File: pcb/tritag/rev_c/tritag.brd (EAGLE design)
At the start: 61 x 34.5 mm, 139 parts, among them J1 TC2030-JLINK-NL, J2 TC2030-JLINK-NL, J3 MICRO_USB_B_HIROSE_ZX62-B-5PA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, J5 BAT_HOLE, J7 CON_MICRO_SDDM3AT-SF-PEJM5, T1 HHM1595A1, U1 NRF52840, U12 SIP32510, U2 MCP73831, U3 FT232RQ, U4 MAX8887EZK33+T, U5 STM32F091CC, U6 SKY13317, U7 LXDC2HN18A, U8 DW1000, U9 LIS2DW12, X1 32MHz, X2 38.4M, X3 16M, X4 32.768kHz

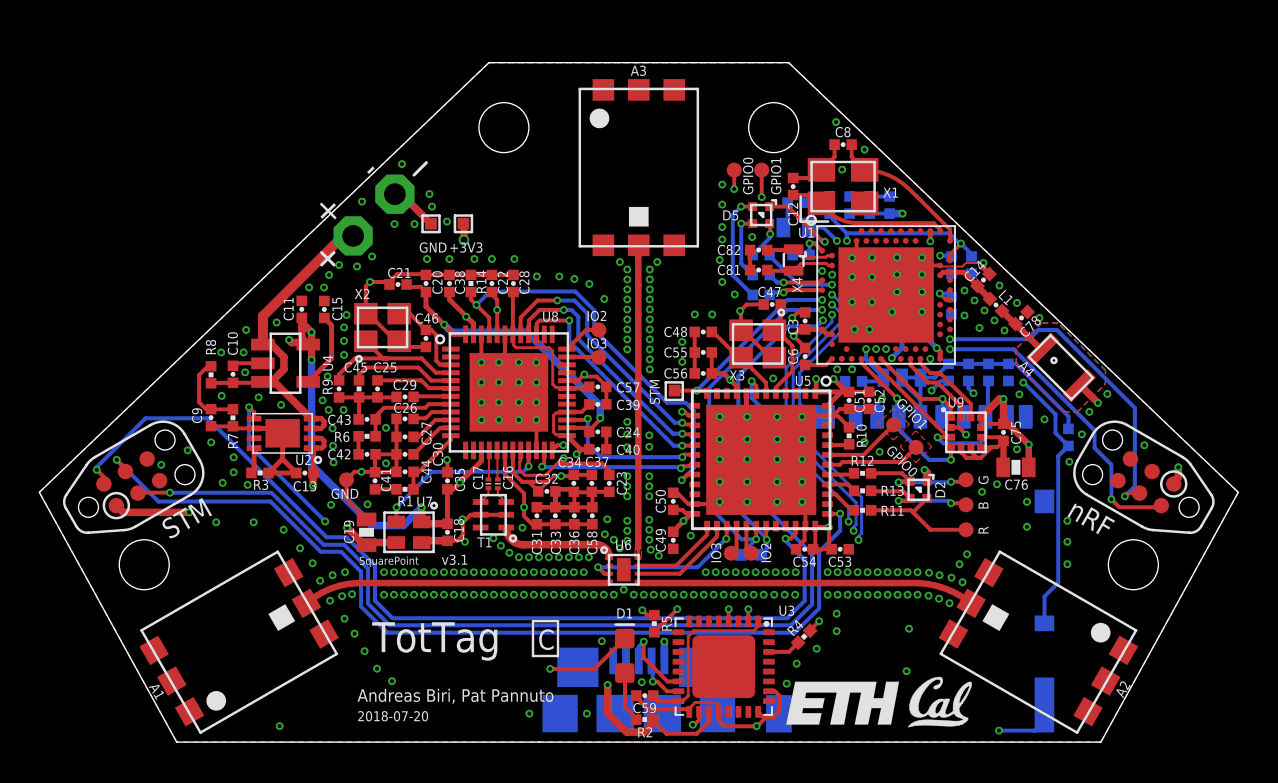
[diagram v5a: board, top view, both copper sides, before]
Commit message: renumbered parts, added decaps for power supply
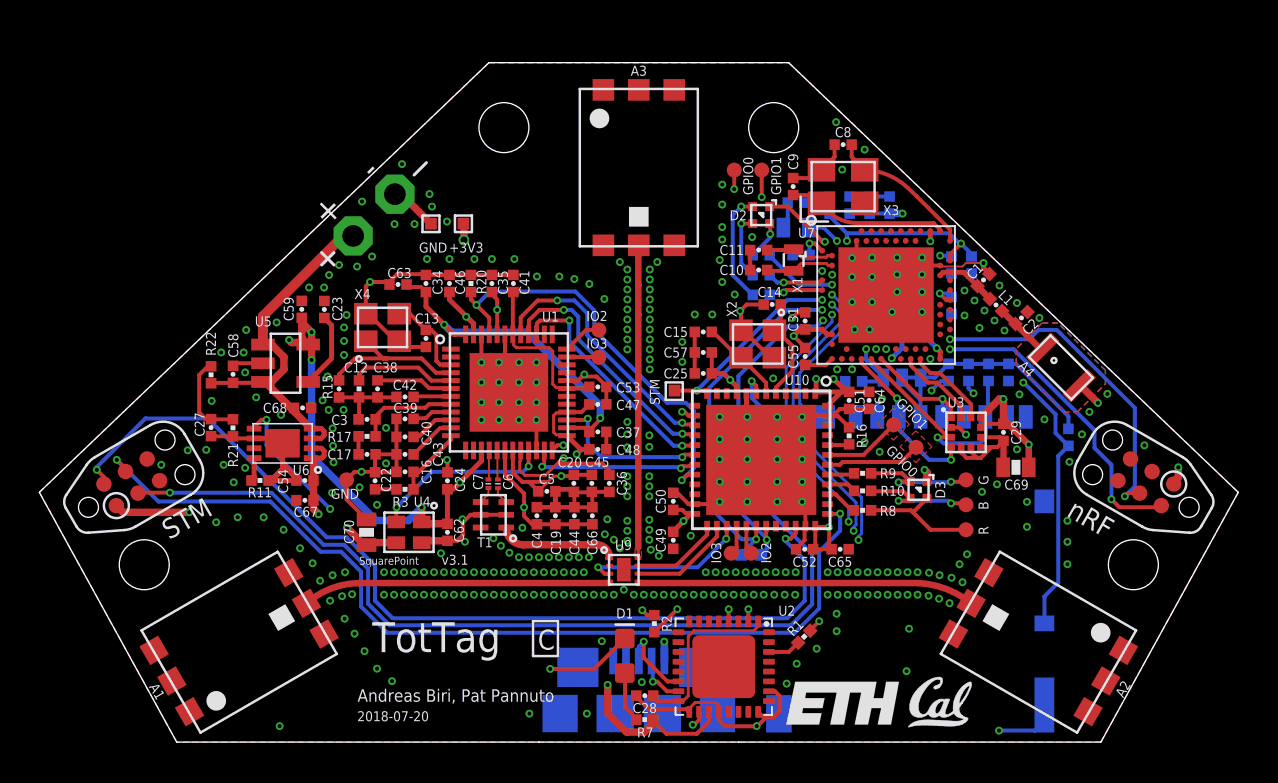
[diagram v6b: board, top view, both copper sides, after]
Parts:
- removed C75: 0.1uF, passives:0402_CAP
- removed C77: 4.7uF, passives:0402_CAP
- removed C78: 1pF, passives:0402_CAP
- removed C79: 1uF, passives:0402_CAP
- removed C80: 47nF, passives:0402_CAP
- removed C81, C82: 12pF, passives:0402_CAP
- removed D5: SML-LX0404SIUPGUSB, leds:1MM_SQ_4PAD
- removed J7: CON_MICRO_SDDM3AT-SF-PEJM5, connector:DM3AT-SF-PEJM5
- removed R23: 10k, passives:0402_RES
- removed R27, R28, R29: 470, passives:0402_RES
- removed U12: SIP32510, chips:TSOT23-6
- added C61, C62, C63, C64, C65, C66, C67, C68: 4.7uF, passives:0402_CAP
- added C70: 10uF, passives:0603_CAP
- added D3: SML-LX0404SIUPGUSB, leds:1MM_SQ_4PAD
- added J4: TC2030-JLINK-NL, connector:TC2030-IDC-NL
- added R15: 11k 1%, passives:0402_RES
- added R16: 11k, passives:0402_RES
- added R17: 16k, passives:0402_RES
- added R18: 100k, passives:0402_RES
- added U10: STM32F091CC, chips:UFQFPN-48
- C1: value 4.7uF -> 1pF
- C10, C11: value 4.7uF -> 12pF
- C13: value 1uF -> 12pF
- C14: value 1pF -> 12pF
- C15: value 10nF -> 12pF
- C16: value 12pF -> 18pF; device passives:0201_CAP -> passives:0402_CAP
- C17: value 12pF -> 27pF; device passives:0201_CAP -> passives:0402_CAP
- C18: value 4.7uF -> 100pF
- C19: value 10uF -> 330pF; device passives:0603_CAP -> passives:0402_CAP
- C2: value 0.1uF -> 1pF
- C20: value 0.1uF -> 330pF
- C21: value 4.7uF -> 820pF
- C22: value 0.1uF -> 820pF
- C23, C24, C25: value 0.1uF -> 10nF
- C26: value 0.1uF -> 47nF
- C3: value 0.1uF -> 1.2pF
- C31, C32: value 10pF -> 0.1uF
- C33, C34: value 330pF -> 0.1uF
- C35: value 0.01uF -> 0.1uF
- C4, C5: value 0.1uF -> 10pF
- C41: value 820pF -> 0.1uF
- C42: value 27pF -> 0.1uF
- C43: value 1.2pF -> 0.1uF
- C44: value 18pF -> 0.1uF
- C45, C46, C47, C48: value 12pF -> 0.1uF
- C49, C50, C51: value 100nF -> 0.1uF
- C52, C53: value 4.7uF -> 0.1uF
- C54: value 100nF -> 1uF
- C56: value 10nF -> 1uF
- C57: value 0.1uF -> 1uF
- C59: value 0.1uF -> 4.7uF
- C6: value 1uF -> 12pF; device passives:0402_CAP -> passives:0201_CAP
- C60: value 820pF -> 4.7uF
- C7: value 100pF -> 12pF; device passives:0402_CAP -> passives:0201_CAP
- C9: value 0.1uF -> 12pF
- J1: value TC2030-JLINK-NL -> BAT_HOLE; device connector:TC2030-IDC-NL -> connector:BATTERY_HOLE
- J2: value TC2030-JLINK-NL -> CON_MICRO_SDDM3AT-SF-PEJM5; device connector:TC2030-IDC-NL -> connector:DM3AT-SF-PEJM5
- J5: value BAT_HOLE -> TC2030-JLINK-NL; device connector:BATTERY_HOLE -> connector:TC2030-IDC-NL
- R1: value 270 -> 0
- R10: value 11k -> 1k
- R11: value 1k -> 2k 1%
- R12, R13: value 1k -> 10k
- R14: value 100k -> 10k
- R2: value 1k -> 0
- R21: value 10k -> 2.2M
- R22: value 10k -> 10M
- R3: value 2k 1% -> 270
- R4, R5: value 0 -> 470
- R6: value 16k -> 470
- R7: value 2.2M -> 1k
- R8: value 10M -> 1k
- R9: value 11k 1% -> 1k
- U1: value NRF52840 -> DW1000; device chips:AQFN73 -> chips:QFN-48-DW1000
- U2: value MCP73831 -> FT232RQ; device chips:DFN-8-MCP -> ftdichip:QFN32
- U3: value FT232RQ -> LIS2DW12; device ftdichip:QFN32 -> chips:LGA-12
- U4: value MAX8887EZK33+T -> LXDC2HN18A; device chips:SOT-23-5 -> regulators:LXDC2HN
- U5: value STM32F091CC -> MAX8887EZK33+T; device chips:UFQFPN-48 -> chips:SOT-23-5
- U6: value SKY13317 -> MCP73831; device switches:MLPQ-UT-8 -> chips:DFN-8-MCP
- U7: value LXDC2HN18A -> NRF52840; device regulators:LXDC2HN -> chips:AQFN73
- U8: value DW1000 -> SIP32510; device chips:QFN-48-DW1000 -> chips:TSOT23-6
- U9: value LIS2DW12 -> SKY13317; device chips:LGA-12 -> switches:MLPQ-UT-8
- X1: value 32MHz -> 32.768kHz; device crystals:TXC-7V -> crystals:ABS05
- X2: value 38.4M -> 16MHz
- X3: value 16M -> 32MHz; device crystals:FA-20H -> crystals:TXC-7V
- X4: value 32.768kHz -> 38.4MHz; device crystals:ABS05 -> crystals:FA-20H
- moved J1 41.5 mm to (-13.5, 23.0), turned to 45 degrees
- moved J2 40.2 mm to (14.2, 12.8), flipped to the bottom, turned to 0 degrees
- moved R22 38.5 mm to (-21.7, 14.9), flipped to the top, turned to 270 degrees
- moved R21 36.5 mm to (-20.6, 12.2), flipped to the top
- moved R8 33.8 mm to (11.4, 7.98), turned to 180 degrees
- moved C9 31.8 mm to (7.85, 24.4), turned to 270 degrees
- moved R20 31.4 mm to (-8.53, 19.5), flipped to the top, turned to 270 degrees
- moved R11 30.7 mm to (-19.3, 9.49)
- moved C29 30.5 mm to (18.5, 11.9), turned to 270 degrees
- moved C26 29.8 mm to (16.9, 20.4), flipped to the bottom, turned to 270 degrees
- moved C18 29.0 mm to (15.9, 20.4), flipped to the bottom, turned to 270 degrees
- moved C21 28.2 mm to (15.9, 18.4), flipped to the bottom, turned to 270 degrees
- moved C30 27.7 mm to (12.8, 23.5), flipped to the bottom, turned to 90 degrees
- moved C10 27.2 mm to (6.10, 20.2), turned to 0 degrees
- moved U7 27.1 mm to (12.6, 18.9), turned to 0 degrees
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- renumbered C76 to C69
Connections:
- net !CHRG: now also R7.1; no longer R2.1
- net !DW_RST: now also U1.27, U10.18; no longer U5.18, U8.27
- net !DW_SPI_CS: now also U1.24, U10.14; no longer U5.14, U8.24
- net !FT_RST: now also U2.18, U7.P2; no longer U1.P2, U3.18
- net !NRF_CS_IMU: now also U3.2, U7.AC11; no longer U1.AC11, U9.2
- net !NRF_CS_SD: now also J2.2, R13.1, U7.AC13; no longer J7.2, R22.1, U1.AC13
- net !SD_DETECT: now also J2.A, R19.1, U7.AD22; no longer J7.A, R20.1, U1.AD22
- net !STM_RST: now also J5.3, U10.7; no longer J2.3, U5.7
- net +1V8: now also C34.1, C37.1, C63.1, C70.1, U1.26, U1.48, U4.3; no longer C19.1, C20.1, C21.1, C24.1, U7.3, U8.26, U8.48
- net +3V3: now also C19.1, C20.1, C24.1, C25.1, C29.1, C30.1, C4.1, C44.1, C45.1, C46.1, C47.1, C48.1, C57.1, C59.1, C61.1, C62.2, C64.1, C65.1, C66.1, D3.1, J4.1, J5.1, U1.15, U1.18, U1.19, U1.25, U1.28, U1.47, U10.1, U10.24, U10.36, U10.48, U10.9, U3.10, U3.9, U4.1, U5.5, U7.A22, U7.AD14, U7.AD23, U7.B1, U7.W1, U7.Y2, U8.5, U8.6; no longer C1.1, C11.1, C18.2, C2.1, C3.1, C32.1, C34.1, C35.1, C36.1, C37.1, C38.1, C39.1, C40.1, C53.1, C54.1, C56.1, C58.1, C6.1, C75.1, D5.1, J1.1, J2.1, U1.A22, U1.AD14, U1.AD23, U1.B1, U1.W1, U1.Y2, U12.5, U12.6, U4.5, U5.1, U5.24, U5.36, U5.48, U5.9, U7.1, U8.15, U8.18, U8.19, U8.25, U8.28, U8.47, U9.10, U9.9
- net ANT_SEL1: now also U10.27, U9.3; no longer U5.27, U6.3
- net ANT_SEL2: now also U10.26, U9.6; no longer U5.26, U6.6
- net ANT_SEL3: now also U10.25, U9.7; no longer U5.25, U6.7
- net BATIN: now also C27.2, R21.2, R22.1; no longer C9.2, R7.2, R8.1
- net D+: now also U2.14; no longer U3.14
- net D-: now also U2.15; no longer U3.15
- net DBG_RX: now also R1.2, U7.M2; no longer R4.2, U1.M2
- net DBG_TX: now also R2.2, U7.T2; no longer R5.2, U1.T2
- net DW_IRQ: now also R20.2, U1.45, U10.20; no longer R14.2, U5.20, U8.45
- net DW_SPI_CLK: now also U1.41, U10.15; no longer U5.15, U8.41
- net DW_SPI_MISO: now also U1.40, U10.16; no longer U5.16, U8.40
- net DW_SPI_MOSI: now also U1.39, U10.17; no longer U5.17, U8.39
- net DW_SYNC: now also U1.29; no longer U8.29
- net DW_WAKEUP: now also U1.23, U10.19; no longer U5.19, U8.23
- net EXT_I2C_SCL: now also U10.30, U7.R1; no longer U1.R1, U5.30
- net EXT_I2C_SDA: now also U10.31, U7.U1; no longer U1.U1, U5.31
- net GND: now also C10.1, C11.1, C12.2, C16.2, C17.2, C18.2, C27.1, C61.2, C62.1, C63.2, C64.2, C65.2, C66.2, C67.2, C68.2, C70.2, J1.N, J2.6, J2.B, J2.MOUNT0, J2.MOUNT1, J2.MOUNT2, J2.MOUNT3, J4.5, J5.5, R11.1, R15.1, R16.2, R18.2, R20.1, R21.1, U1.22, U1.32, U1.43, U1.46, U10.23, U10.35, U10.47, U10.8, U10.GND, U2.17, U2.20, U2.24, U2.26, U2.4, U3.5, U3.6, U3.7, U3.8, U4.4, U5.2, U6.6, U7.AD2, U7.B7, U7.F23, U7.GND, U8.4, U9.GND, X4.2, X4.4; no longer C10.2, C11.2, C12.1, C18.1, C27.2, C6.2, C7.2, C75.2, C77.2, C78.2, C79.2, C80.2, C81.1, C82.1, J1.5, J2.5, J5.N, J7.6, J7.B, J7.MOUNT0, J7.MOUNT1, J7.MOUNT2, J7.MOUNT3, R10.2, R14.1, R19.2, R3.1, R7.1, R9.1, U1.AD2, U1.B7, U1.F23, U12.4, U2.6, U2.GND, U3.17, U3.20, U3.24, U3.26, U3.4, U4.2, U5.23, U5.35, U5.47, U5.8, U5.GND, U7.4, U8.22, U8.32, U8.43, U8.46, U8.GND, U9.5, U9.6, U9.7, U9.8, X1.2, X1.4
- net GPIO0: now also U10.42; no longer U5.42
- net GPIO1: now also U10.43; no longer U5.43
- net GPIO2: now also U10.29; no longer U5.29
- net GPIO3: now also U10.28; no longer U5.28
- net LED_BLUE: now also R10.2, U10.40; no longer R13.2, U5.40
- net LED_GREEN: now also R9.2, U10.41; no longer R12.2, U5.41
- net LED_NRF_BLUE: now also R6.2, U7.J1; no longer R29.2, U1.J1
- net LED_NRF_GREEN: now also R5.2, U7.L1; no longer R28.2, U1.L1
- net LED_NRF_RED: now also R4.2, U7.K2; no longer R27.2, U1.K2
- net LED_RED: now also R8.2, U10.39; no longer R11.2, U5.39
- net N$1: now also C28.1, U2.1, U2.16; no longer C59.1, U3.1, U3.16
- net N$10: now also C18.1, U7.D23; no longer C7.1, U1.D23
- net N$11: now also C23.1, U5.4; no longer C15.1, U4.4
- net N$12: now also C17.1, R17.2; no longer C42.1, R6.2
- net N$13: now also R11.2, U6.8; no longer R3.2, U2.8
- net N$14: now also C16.1, R3.1, U1.12; no longer C44.1, R1.1, U8.12
- net N$15: now also C1.1, U7.H23; no longer C14.1, U1.H23
- net N$16: now also C3.1, R17.1, U1.8; no longer C43.1, R6.1, U8.8
- net N$17: now also C2.1; no longer C78.1
- net N$18: now also U7.B24, X3.3; no longer U1.B24, X1.3
- net N$19: now also C9.2, U7.A23, X3.1; no longer C12.2, U1.A23, X1.1
- net N$2: now also C21.1, U7.N24; no longer C60.1, U1.N24
- net N$20: now also U7.B3; no longer U1.B3
- net N$21: now also R15.2, U1.5; no longer R9.2, U8.5
- net N$22: now also R16.1, U10.44; no longer R10.1, U5.44
- net N$23: now also D3.4, R9.1; no longer D2.4, R12.1
- net N$24: now also D3.3, R10.1; no longer D2.3, R13.1
- net N$25: now also D3.2, R8.1; no longer D2.2, R11.1
- net N$26: now also U1.36; no longer U8.36
- net N$27: now also U1.35; no longer U8.35
- net N$3: now also U9.1; no longer U6.1
- net N$33: now also R1.1, U2.30; no longer R4.1, U3.30
- net N$34: now also R2.1, U2.2; no longer R5.1, U3.2
- net N$4: now also C6.P$2; no longer C16.P$2
- net N$5: now also U6.5; no longer U2.5
- net N$55: now also C60.1, J2.4, R12.2, R13.2, R14.2, R19.2, U8.1, U8.2; no longer C77.1, J7.4, R20.2, R21.2, R22.2, R23.2, U12.1, U12.2
- net N$59: now also D2.2, R4.1; no longer D5.2, R27.1
- net N$6: now also C32.1, U7.C1; no longer C4.1, U1.C1
- net N$60: now also D2.4, R5.1; no longer D5.4, R28.1
- net N$61: now also D2.3, R6.1; no longer D5.3, R29.1
- net N$7: now also C7.P$2; no longer C17.P$2
- net N$8: now also C22.1, R3.2; no longer C41.1, R1.2
- net N$9: now also C26.1, C56.1, U7.B5, U7.E24; no longer C79.1, C80.1, U1.B5, U1.E24
- net NRF_GPIO_0: now also U7.H2; no longer U1.H2
- net NRF_GPIO_1: now also U7.G1; no longer U1.G1
- net NRF_IMU_INT1: now also U3.12, U7.AD18; no longer U1.AD18, U9.12
- net NRF_IMU_INT2: now also U3.11, U7.AD20; no longer U1.AD20, U9.11
- net NRF_MISO: now also J2.7, R14.1, U3.3, U7.AD10; no longer J7.7, R23.1, U1.AD10, U9.3
- net NRF_MOSI: now also J2.3, R12.1, U3.4, U7.AD8; no longer J7.3, R21.1, U1.AD8, U9.4
- net NRF_SCK: now also J2.5, U3.1, U7.AD12; no longer J7.5, U1.AD12, U9.1
- net NRF_SWDCLK: now also J4.4, U7.AA24; no longer J1.4, U1.AA24
- net NRF_SWDIO: now also J4.2, U7.AC24; no longer J1.2, U1.AC24
- net OSC_IN: now also C14.1, U10.5, X2.1; no longer C47.1, U5.5, X3.1
- net OSC_OUT: now also C15.1, U10.6, X2.3; no longer C48.1, U5.6, X3.3
- net REG_EN: now also U1.21, U4.2; no longer U7.2, U8.21
- net RF1: now also U9.4; no longer U6.4
- net RF2: now also U9.5; no longer U6.5
- net RF3: now also U9.8; no longer U6.8
- net RF_N: now also C6.P$1, U1.17; no longer C16.P$1, U8.17
- net RF_P: now also C7.P$1, U1.16; no longer C17.P$1, U8.16
- net SD_EN: now also R18.1, U7.AC9, U8.3; no longer R19.1, U1.AC9, U12.3
- net STM_INTERRUPT: now also U10.12, U7.N1; no longer U1.N1, U5.12
- net STM_SWCLK: now also J5.4, U10.37; no longer J2.4, U5.37
- net STM_SWDIO: now also J5.2, U10.34; no longer J2.2, U5.34
- net VBAT: now also C58.1, C68.1, J1.P, R22.2, U5.1, U5.3, U6.3, U6.4; no longer C10.1, J5.P, R8.2, U2.3, U2.4, U4.1, U4.3
- net VDDCLK: now also C39.1, U1.9; no longer C26.1, U8.9
- net VDDDIG: now also C35.1, C36.1, U1.20, U1.44; no longer C22.1, C23.1, U8.20, U8.44
- net VDDIF: now also C42.1, U1.7; no longer C29.1, U8.7
- net VDDIO: now also C41.1, C53.1, U1.31, U1.42; no longer C28.1, C57.1, U8.31, U8.42
- net VDDMS: now also C38.1, U1.6; no longer C25.1, U8.6
- net VDDSYN: now also C40.1, U1.10; no longer C27.1, U8.10
- net VDDVCO: now also C43.1, U1.11; no longer C30.1, U8.11
- net VUSB: now also C54.1, C67.1, R7.2, U2.19, U6.1, U6.2; no longer C13.1, R2.2, U2.1, U2.2, U3.19
- net XL3: now also C11.2, U7.D2, X1.A; no longer C82.2, U1.D2, X4.A
- net XL4: now also C10.2, U7.F2, X1.B; no longer C81.2, U1.F2, X4.B
- net XTAL1: now also C13.1, U1.3, X4.3; no longer C46.1, U8.3, X2.3
- net XTAL2: now also C12.1, U1.4, X4.1; no longer C45.1, U8.4, X2.1
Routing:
- net GND: track 162.1 -> 165.6 mm, vias 351 -> 353
- net VUSB: track 39.2 -> 38.0 mm
- net N$5: track 28.4 -> 27.6 mm
- net BATIN: track 4.05 -> 4.55 mm
